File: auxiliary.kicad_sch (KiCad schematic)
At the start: 67 parts, among them IC1 MAX1708EEE+, J4 BM04B-SRSS-TB-LF-SN, J5 SM06B-SRSS-TB(LF)(SN), J6 SM09B-SRSS-TB(LF)(SN), Q1 BSS138AKA, U1 PCA9547BS,118, U2 NTS0102DP

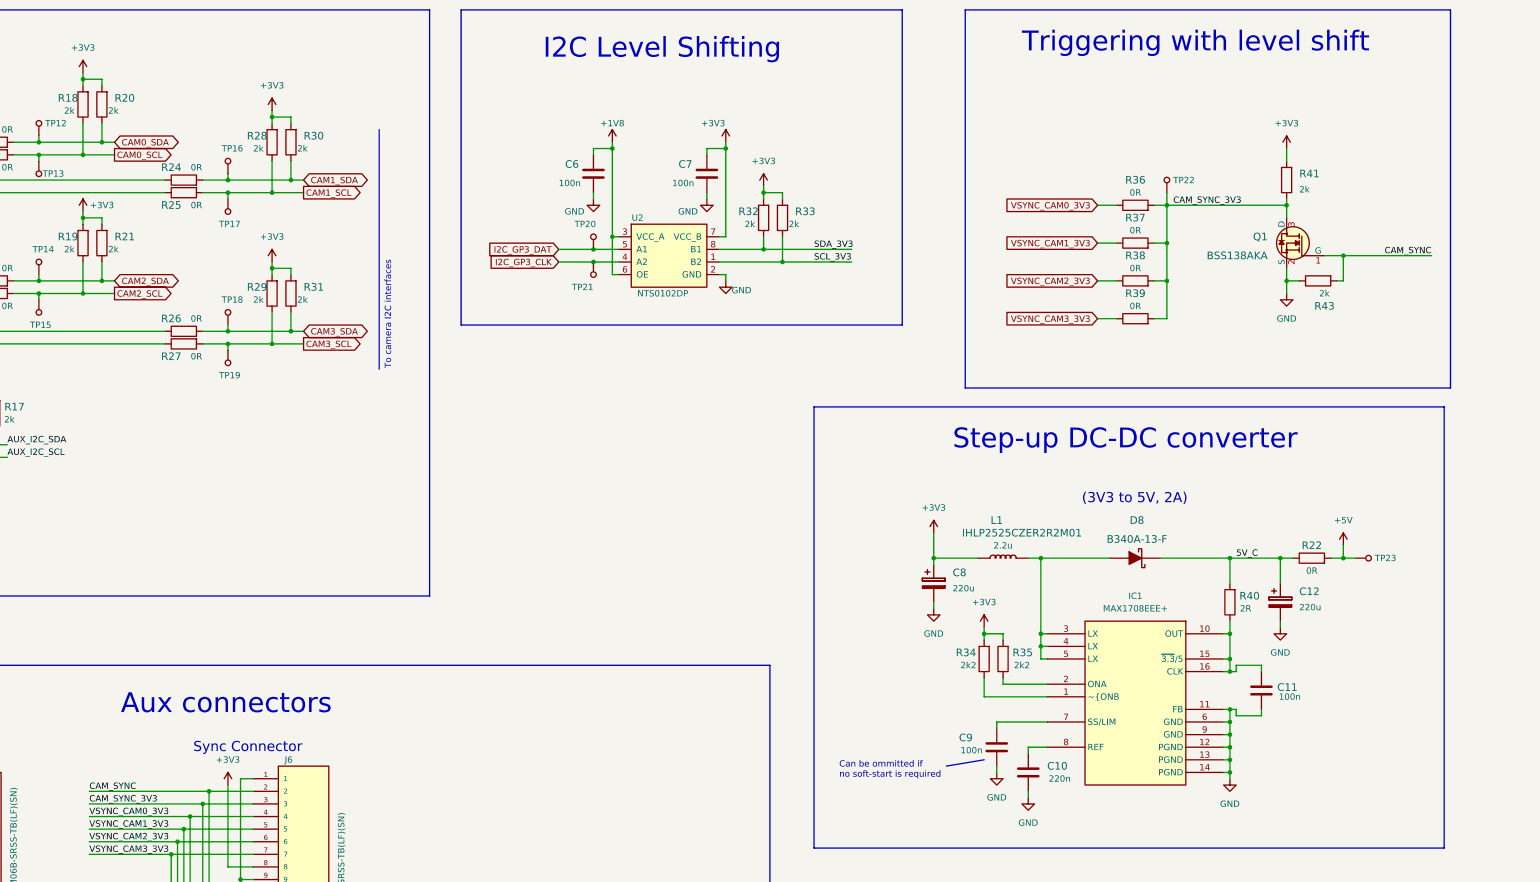
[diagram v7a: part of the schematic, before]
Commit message: Length matched CSI signals
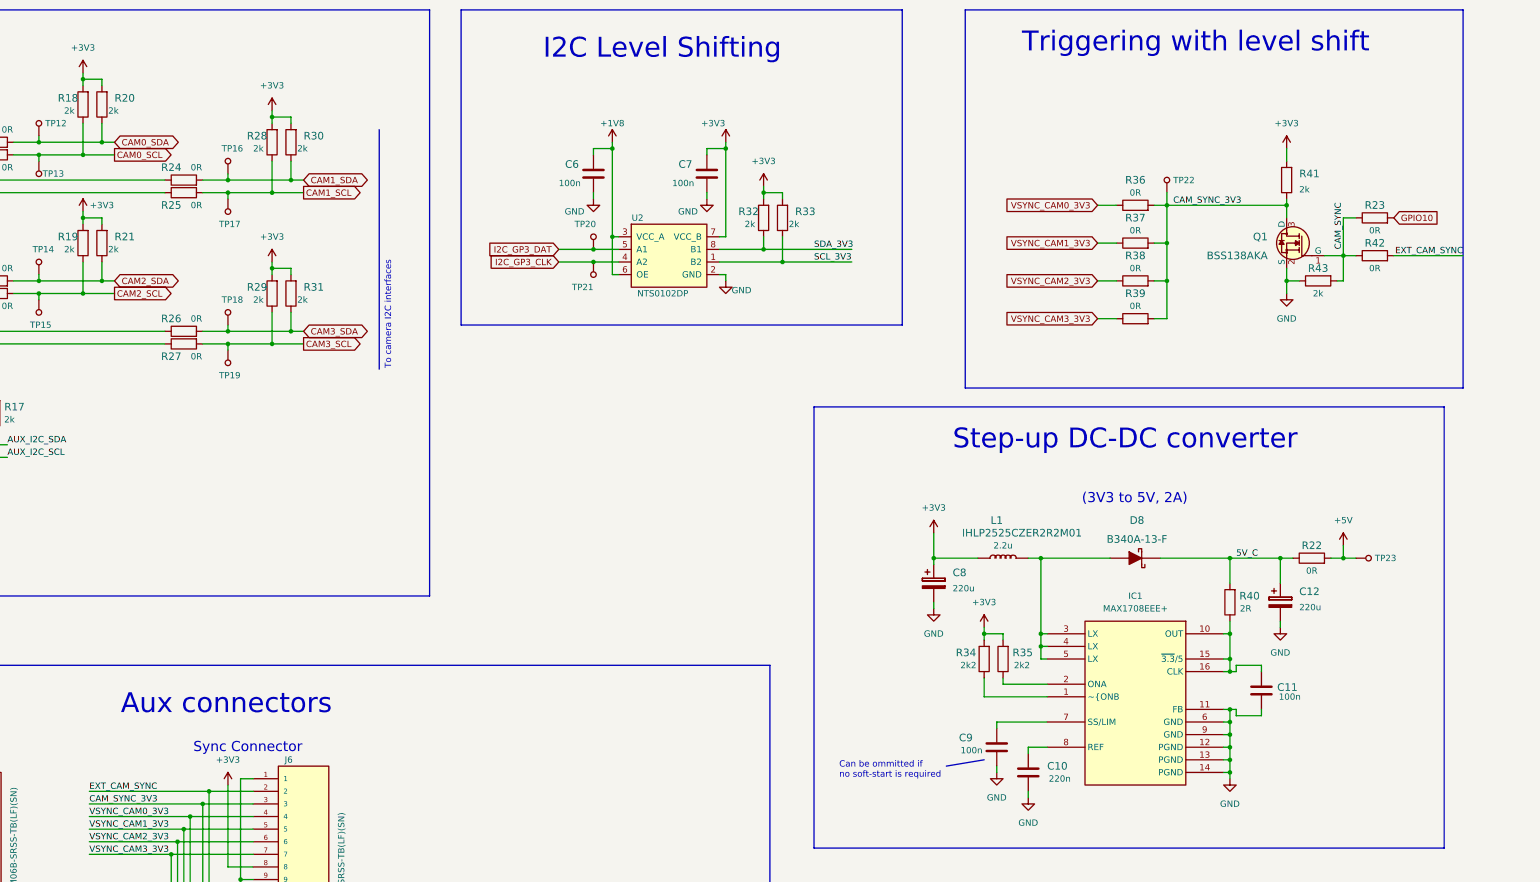
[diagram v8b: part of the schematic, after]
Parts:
- added R23, R42: R_0R_0402, antmicro-footprints:0402-res, symbol antmicroResistors0402:R_0R_0402
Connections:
- net CAM_SYNC: now also R23.1, R42.1; no longer D7.4 (CH3), D7.7 (CH3), J6.2
- new net EXT_CAM_SYNC: D7.4 (CH3), D7.7 (CH3), J6.2, R42.2
- new net GPIO10: R23.2
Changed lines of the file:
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@@
     (stroke (width 0) (type default) (color 0 0 0 0))
   )
-  (polyline (pts (xy 396.24 100.33) (xy 396.24 24.13))
+  (polyline (pts (xy 398.78 100.33) (xy 398.78 24.13))
     (stroke (width 0) (type default) (color 0 0 0 0))
   )
@@
     (stroke (width 0) (type default) (color 0 0 0 0))
   )
+  (wire (pts (xy 384.81 73.66) (xy 398.78 73.66))
+    (stroke (width 0) (type default) (color 0 0 0 0))
+  )
   (wire (pts (xy 227.33 69.85) (xy 227.33 77.47))
     (stroke (width 0) (type default) (color 0 0 0 0))
@@
     (stroke (width 0) (type default) (color 0 0 0 0))
   )
-  (polyline (pts (xy 298.45 24.13) (xy 396.24 24.13))
+  (polyline (pts (xy 298.45 24.13) (xy 398.78 24.13))
     (stroke (width 0) (type default) (color 0 0 0 0))
   )
@@
     (stroke (width 0) (type default) (color 0 0 0 0))
   )
+  (wire (pts (xy 377.19 66.04) (xy 374.65 66.04))
+    (stroke (width 0) (type default) (color 0 0 0 0))
+  )
   (wire (pts (xy 99.06 100.33) (xy 99.06 101.6))
     (stroke (width 0) (type default) (color 0 0 0 0))
@@
     (stroke (width 0) (type default) (color 0 0 0 0))
   )
+  (wire (pts (xy 374.65 66.04) (xy 374.65 73.66))
+    (stroke (width 0) (type default) (color 0 0 0 0))
+  )
   (wire (pts (xy 257.81 60.96) (xy 257.81 62.23))
     (stroke (width 0) (type default) (color 0 0 0 0))
@@
     (stroke (width 0) (type default) (color 0 0 0 0))
   )
-  (wire (pts (xy 374.65 73.66) (xy 392.43 73.66))
-    (stroke (width 0) (type default) (color 0 0 0 0))
-  )
   (wire (pts (xy 106.68 78.74) (xy 111.76 78.74))
     (stroke (width 0) (type default) (color 0 0 0 0))
@@
     (stroke (width 0) (type default) (color 0 0 0 0))
   )
-  (polyline (pts (xy 298.45 100.33) (xy 396.24 100.33))
+  (polyline (pts (xy 298.45 100.33) (xy 398.78 100.33))
     (stroke (width 0) (type default) (color 0 0 0 0))
   )
@@
     (stroke (width 0) (type default) (color 0 0 0 0))
   )
+  (wire (pts (xy 374.65 73.66) (xy 377.19 73.66))
+    (stroke (width 0) (type default) (color 0 0 0 0))
+  )
   (wire (pts (xy 55.88 119.38) (xy 53.34 119.38))
     (stroke (width 0) (type default) (color 0 0 0 0))
@@
     (effects (font (size 1.27 1.27)) (justify left bottom))
   )
+  (label "EXT_CAM_SYNC" (at 121.92 181.61 0)
+    (effects (font (size 1.27 1.27)) (justify left bottom))
+  )
   (label "AUX_I2C_SCL" (at 36.83 187.96 0)
     (effects (font (size 1.27 1.27)) (justify left bottom))
@@
     (effects (font (size 1.27 1.27)) (justify left bottom))
   )
+  (label "CAM_SYNC" (at 374.65 72.39 90)
+    (effects (font (size 1.27 1.27)) (justify left bottom))
+  )
   (label "SCL_3V3" (at 34.29 83.82 0)
     (effects (font (size 1.27 1.27)) (justify left bottom))
@@
     (effects (font (size 1.27 1.27)) (justify left bottom))
   )
-  (label "CAM_SYNC" (at 392.43 73.66 180)
+  (label "EXT_CAM_SYNC" (at 398.78 73.66 180)
     (effects (font (size 1.27 1.27)) (justify right bottom))
   )
@@
     (effects (font (size 1.27 1.27)) (justify left bottom))
   )
-  (label "CAM_SYNC" (at 121.92 181.61 0)
-    (effects (font (size 1.27 1.27)) (justify left bottom))
-  )
   (global_label "VSYNC_CAM2_3V3" (shape input) (at 325.12 78.74 180) (fields_autoplaced)
     (effects (font (size 1.27 1.27)) (justify right))
@@
     )
   )
+  (global_label "GPIO10" (shape input) (at 384.81 66.04 0) (fields_autoplaced)
+    (effects (font (size 1.27 1.27)) (justify left))
+    (property "Intersheet References" "${INTERSHEET_REFS}" (id 0) (at 394.1174 66.1194 0)
+      (effects (font (size 1.27 1.27)) (justify left) hide)
+    )
+  )
   (global_label "CAM3_SCL" (shape input) (at 80.01 187.96 180) (fields_autoplaced)
     (effects (font (size 1.27 1.27)) (justify right))
@@
   (symbol (lib_id "antmicroResistors0402:R_2k_0402") (at 369.57 78.74 0) (mirror x) (unit 1)
     (in_bom yes) (on_board yes)
-    (property "Reference" "R43" (id 0) (at 370.84 83.82 0)
+    (property "Reference" "R43" (id 0) (at 369.57 76.2 0)
       (effects (font (size 1.524 1.524)))
     )
@@
       (effects (font (size 1.524 1.524)) (justify left) hide)
     )
-    (property "Val" "2k" (id 6) (at 370.84 81.28 0))
+    (property "Val" "2k" (id 6) (at 369.57 81.28 0))
     (pin "1")
     (pin "2")
@@
     (pin "1")
   )
+  (symbol (lib_id "antmicroResistors0402:R_0R_0402") (at 381 66.04 0) (unit 1)
+    (in_bom yes) (on_board yes)
+    (property "Reference" "R23" (id 0) (at 381 63.5 0)
+      (effects (font (size 1.524 1.524)))
+    )
+    (property "Value" "R_0R_0402" (id 1) (at 381 69.85 0)
+      (effects (font (size 1.524 1.524)) hide)
+    )
+    (property "Footprint" "antmicro-footprints:0402-res" (id 2) (at 386.08 60.96 0)
+      (effects (font (size 1.524 1.524)) (justify left) hide)
+    )
+    (property "Datasheet" "" (id 3) (at 381 66.04 0)
+      (effects (font (size 1.27 1.27)) hide)
+    )
+    (property "Manufacturer" "PANASONIC" (id 4) (at 386.08 55.88 0)
+      (effects (font (size 1.524 1.524)) (justify left) hide)
+    )
+    (property "MPN" "ERJ2GE0R00X" (id 5) (at 386.08 58.42 0)
+      (effects (font (size 1.524 1.524)) (justify left) hide)
+    )
+    (property "Val" "0R" (id 6) (at 381 68.58 0))
+    (pin "1")
+    (pin "2")
+  )
   (symbol (lib_id "power:GND") (at 87.63 229.87 0) (unit 1)
     (in_bom yes) (on_board yes) (fields_autoplaced)
@@
     (pin "1")
   )
+  (symbol (lib_id "antmicroResistors0402:R_0R_0402") (at 381 73.66 0) (unit 1)
+    (in_bom yes) (on_board yes)
+    (property "Reference" "R42" (id 0) (at 381 71.12 0)
+      (effects (font (size 1.524 1.524)))
+    )
+    (property "Value" "R_0R_0402" (id 1) (at 381 77.47 0)
+      (effects (font (size 1.524 1.524)) hide)
+    )
+    (property "Footprint" "antmicro-footprints:0402-res" (id 2) (at 386.08 68.58 0)
+      (effects (font (size 1.524 1.524)) (justify left) hide)
+    )
+    (property "Datasheet" "" (id 3) (at 381 73.66 0)
+      (effects (font (size 1.27 1.27)) hide)
+    )
+    (property "Manufacturer" "PANASONIC" (id 4) (at 386.08 63.5 0)
+      (effects (font (size 1.524 1.524)) (justify left) hide)
+    )
+    (property "MPN" "ERJ2GE0R00X" (id 5) (at 386.08 66.04 0)
+      (effects (font (size 1.524 1.524)) (justify left) hide)
+    )
+    (property "Val" "0R" (id 6) (at 381 76.2 0))
+    (pin "1")
+    (pin "2")
+  )
   (symbol (lib_id "antmicroResistors0402:R_2k_0402") (at 158.75 81.28 90) (unit 1)
